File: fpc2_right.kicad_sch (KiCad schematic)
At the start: 6 parts, among them J2432 right power loom, straight-nu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, J2444 main ground strap, J2446 main ground strap

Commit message: start switching the carrier to mu ultra
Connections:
- net TCP0_DDC_SCL renamed TCP2_DDC_SCL
- net TCP0_DDC_SDA renamed TCP2_DDC_SDA
- net TCP0_HPD renamed TCP2_HPD
- net TCP0_TX0_N renamed TCP2_TX0_N
- net TCP0_TX0_P renamed TCP2_TX0_P
- net TCP0_TX1_N renamed TCP2_TX1_N
- net TCP0_TX1_P renamed TCP2_TX1_P
- net TCP0_TXRX0_N renamed TCP2_TXRX0_N
- net TCP0_TXRX0_P renamed TCP2_TXRX0_P
- net TCP0_TXRX1_N renamed TCP2_TXRX1_N
- net TCP0_TXRX1_P renamed TCP2_TXRX1_P
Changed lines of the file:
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@@
   (effects (font (size 1.27 1.27)) (justify right bottom))
 )
-(hierarchical_label "TCP0_HPD"
+(hierarchical_label "TCP2_HPD"
   (shape bidirectional)
   (at 54.61 350.52 180)
   (effects (font (size 1.27 1.27)) (justify right bottom))
 )
-(hierarchical_label "TCP0_DDC_SDA"
+(hierarchical_label "TCP2_DDC_SDA"
   (shape bidirectional)
   (at 54.61 353.06 180)
   (effects (font (size 1.27 1.27)) (justify right bottom))
 )
-(hierarchical_label "TCP0_DDC_SCL"
+(hierarchical_label "TCP2_DDC_SCL"
   (shape bidirectional)
   (at 54.61 355.6 180)
@@
   (effects (font (size 1.27 1.27)) (justify right bottom))
 )
-(hierarchical_label "TCP0_TXRX1_N"
+(hierarchical_label "TCP2_TXRX1_N"
   (shape bidirectional)
   (at 54.61 398.78 180)
   (effects (font (size 1.27 1.27)) (justify right bottom))
 )
-(hierarchical_label "TCP0_TXRX1_P"
+(hierarchical_label "TCP2_TXRX1_P"
   (shape bidirectional)
   (at 54.61 401.32 180)
   (effects (font (size 1.27 1.27)) (justify right bottom))
 )
-(hierarchical_label "TCP0_TXRX0_N"
+(hierarchical_label "TCP2_TXRX0_N"
   (shape bidirectional)
   (at 54.61 406.4 180)
   (effects (font (size 1.27 1.27)) (justify right bottom))
 )
-(hierarchical_label "TCP0_TXRX0_P"
+(hierarchical_label "TCP2_TXRX0_P"
   (shape bidirectional)
   (at 54.61 408.94 180)
   (effects (font (size 1.27 1.27)) (justify right bottom))
 )
-(hierarchical_label "TCP0_TX1_N"
+(hierarchical_label "TCP2_TX1_N"
   (shape bidirectional)
   (at 54.61 414.02 180)
   (effects (font (size 1.27 1.27)) (justify right bottom))
 )
-(hierarchical_label "TCP0_TX1_P"
+(hierarchical_label "TCP2_TX1_P"
   (shape bidirectional)
   (at 54.61 416.56 180)
   (effects (font (size 1.27 1.27)) (justify right bottom))
 )
-(hierarchical_label "TCP0_TX0_N"
+(hierarchical_label "TCP2_TX0_N"
   (shape bidirectional)
   (at 54.61 421.64 180)
   (effects (font (size 1.27 1.27)) (justify right bottom))
 )
-(hierarchical_label "TCP0_TX0_P"
+(hierarchical_label "TCP2_TX0_P"
   (shape bidirectional)
   (at 54.61 424.18 180)

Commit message: work on the power redesign and case
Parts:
- added J2452: right power rails, ducktop2:WAGO_2060_453_SMD, symbol Connector_Generic:Conn_01x03
- added J2462: right power return, ducktop2:WAGO_2060_451_SMD, symbol Connector_Generic:Conn_01x01
- J2432: value right power loom, straight-numbered -> right power rails; footprint Connector_Molex:Molex_Micro-Fit_3.0_43045-1012_2x05_P3.00mm_Vertical -> ducktop2:WAGO_2060_453_SMD; symbol Connector_Generic:Conn_02x05_Odd_Even -> Connector_Generic:Conn_01x03; Assembly (none) -> strip 7..9 mm; hold the button to insert or remove stranded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; Contacts 43030-0038 tin 18 AWG -> (none); CurrentRatingBasis PS-43045 R; use 12-circuit 18 AWG 5.5 A reference screen; a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 -> 9 A IEC and UL; the 10 A ground-cut screen requires both se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; HarnessPinOrder pin n to pin n; continuity and isolation test every conduct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 -> match rail names in the harness drawing; each three-pole gr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; HarnessWireLength 90..100 mm between crimp barrels, including tolerance -> (none); MPN 43045-1012 -> 2060-453/998-404; Manufacturer Molex -> WAGO; MatedHeight 17.64 mm connector body; current 90..100 mm wire poses requ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 -> 4.5 mm terminal body; wire and release-tool envelopes are s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; MatingHousing 43025-1000 -> (none); ResistanceAcceptance termination <=45 mOhm hot/aged; wire <=30 mOhm/m hot; each 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 -> (none); ReturnAcceptance (none) -> remaining complete braid <=1 mOhm; each return wire >=0.12 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; Wire Alpha Wire 3253 UL1061 18 AWG tinned stranded -> Alpha 6715, 18 AWG 16/30 tinned copper; no ferrule
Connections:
- net GND: now also J2462.1 (Pin_1); no longer J2432.10 (Pin_10), J2432.7 (Pin_7), J2432.8 (Pin_8), J2432.9 (Pin_9)
- net MCU_3V3: now also J2452.1 (Pin_1); no longer J2432.6 (Pin_6)
- net PCIE_3V3: now also J2452.2 (Pin_2); no longer J2432.5 (Pin_5)
- net PD2_VBUS_GATED: now also J2432.3 (Pin_3); no longer J2432.1 (Pin_1)
- net SYS_3V3: now also J2452.3 (Pin_3); no longer J2432.4 (Pin_4)
- net SYS_5V: now also J2432.1 (Pin_1); no longer J2432.3 (Pin_3)

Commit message: rework the board placement and fix more power stuff
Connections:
- net PD2_EFUSE_FAULT_N renamed PD2_EFUSE_PG
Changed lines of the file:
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@@
   (effects (font (size 1.27 1.27)) (justify right bottom))
 )
-(hierarchical_label "PD2_EFUSE_FAULT_N"
+(hierarchical_label "PD2_EFUSE_PG"
   (shape bidirectional)
   (at 54.61 332.74 180)

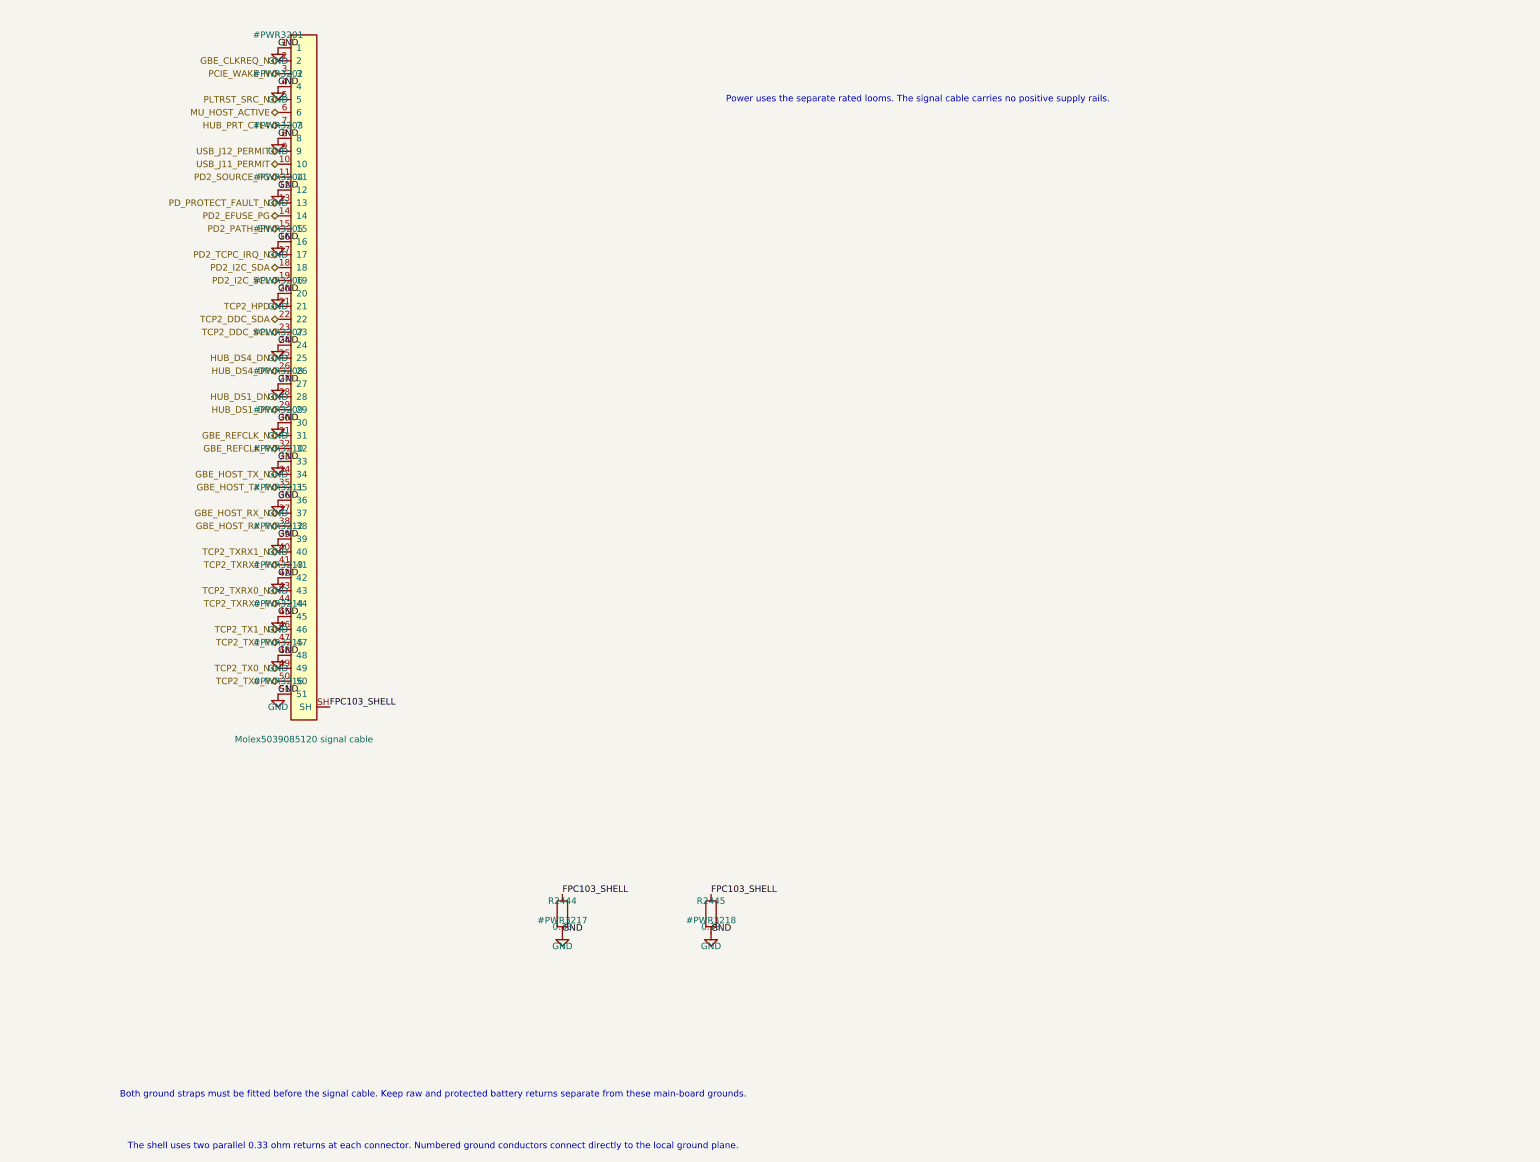
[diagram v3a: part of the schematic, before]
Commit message: finish the new bms and move the connectors up top
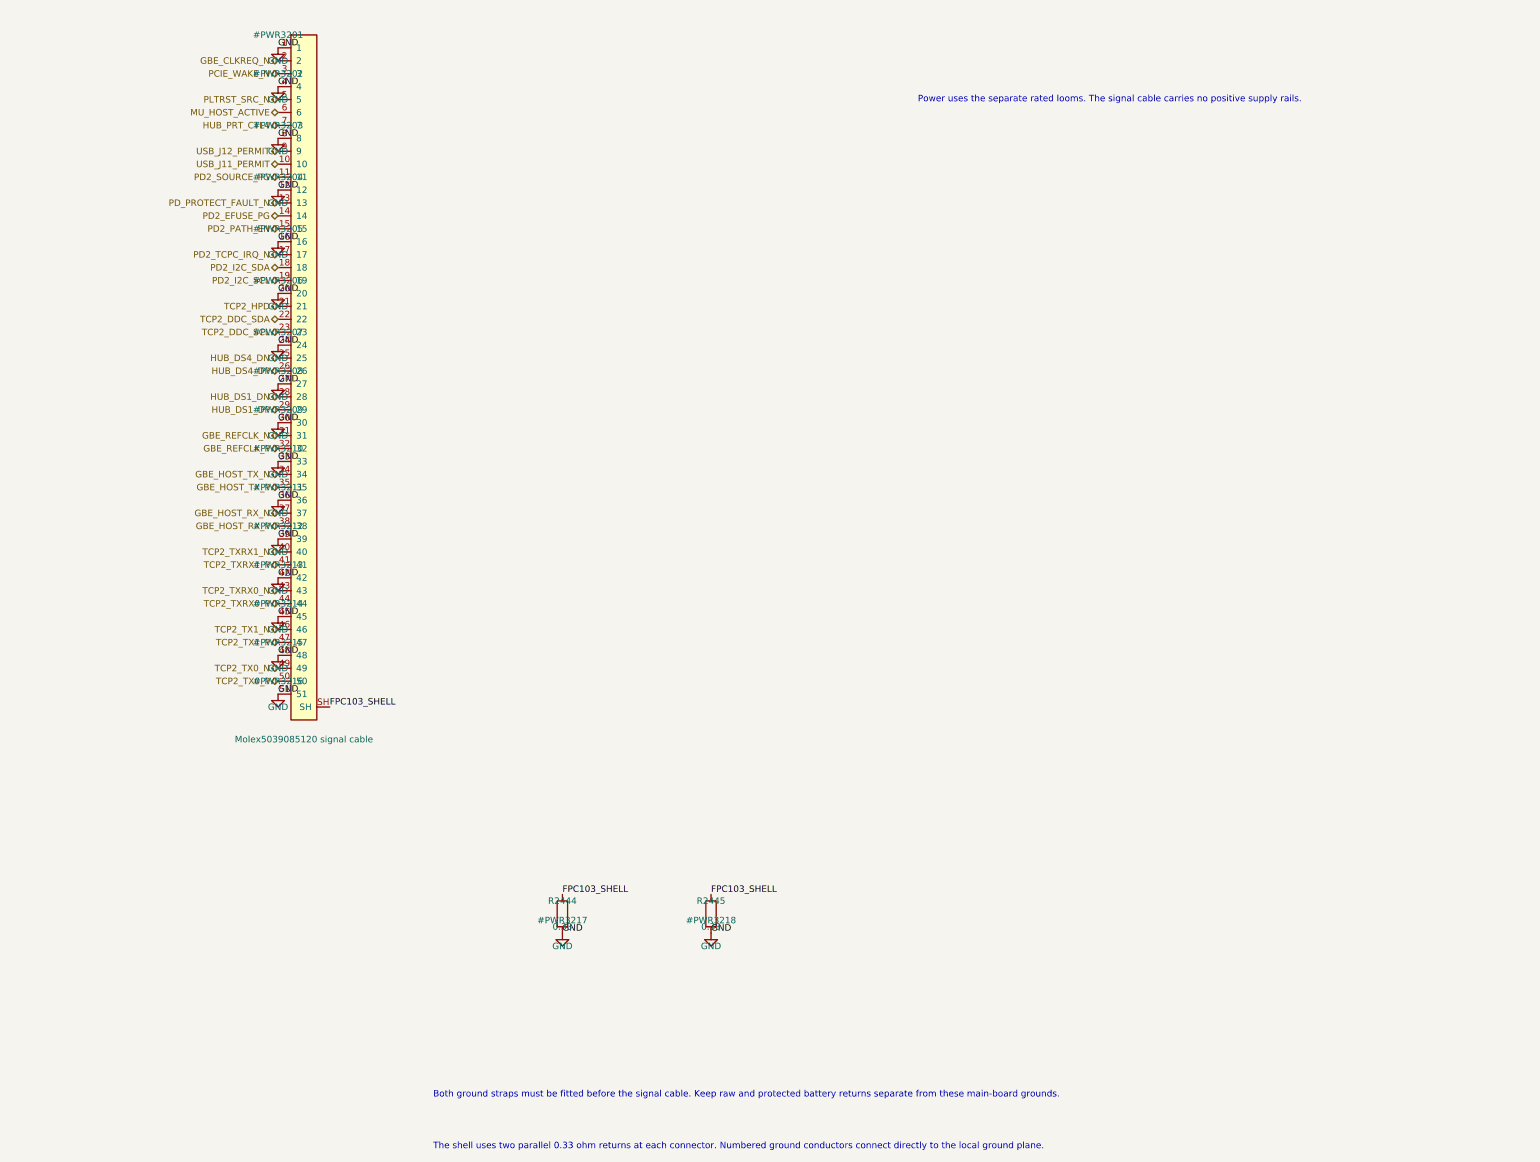
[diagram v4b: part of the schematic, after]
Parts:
- removed J2446: main ground strap, Connector_Wire:SolderWirePad_1x01_SMD_5x10mm, symbol Connector:TestPoint
- added J2444: main ground strap, Connector_Wire:SolderWirePad_1x01_SMD_5x10mm, symbol Connector:TestPoint
- renumbered J2444 to J2446
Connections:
- net GND: now also J2444.1
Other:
- moved on the sheet: J2446
